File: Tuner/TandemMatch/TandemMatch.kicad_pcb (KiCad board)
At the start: 2 copper layers, 100 x 100 mm, 69 parts, among them J1 Conn_01x02, J10 Conn_01x01, J11 Conn_01x01, J12 Conn_01x01, J13 Conn_01x01, J14 Conn_01x01, J15 Conn_01x01, J16 Conn_01x01, J17 Barrel_Jack, J18 Conn_Coaxial, J19 Conn_01x02, J2 Conn_01x02, J20 Conn_Coaxial, J21 Conn_01x01, J22 Conn_01x01, J23 Conn_01x01, J24 Conn_01x01, J25 Conn_01x01, J26 Conn_01x01, J27 Conn_01x01, J28 Conn_01x01, J29 Conn_01x01, J3 Conn_Coaxial, J30 Conn_01x01, J31 Conn_01x01, J32 Conn_01x01, J33 Conn_01x03, J4 Conn_Coaxial, J5 Conn_01x01, J6 Conn_01x01, J7 Conn_01x01, J8 Conn_01x01, J9 Conn_01x01

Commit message: A few tweaks
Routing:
- net Net-(J11-Pad1): track 60.3 -> 59.1 mm
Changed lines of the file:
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@@
   )
   (setup
-    (last_trace_width 2)
+    (last_trace_width 0.25)
     (user_trace_width 0.35)
     (user_trace_width 0.5)
@@
   (segment (start 129.733 59.182) (end 127.447 56.896) (width 2) (layer B.Cu) (net 2))
   (segment (start 127.447 56.896) (end 127.447 56.957) (width 2) (layer B.Cu) (net 2))
-  (segment (start 127.447 56.957) (end 121.904 62.5) (width 2) (layer B.Cu) (net 2))
-  (segment (start 121.904 62.5) (end 110.50524 62.5) (width 2) (layer B.Cu) (net 2))
+  (segment (start 127.447 56.957) (end 113.4745 62.5475) (width 2) (layer B.Cu) (net 2))
+  (segment (start 113.4745 62.5475) (end 110.50524 62.5) (width 2) (layer B.Cu) (net 2))
   (segment (start 123.19 54.102) (end 124.907 54.356) (width 0.5) (layer B.Cu) (net 2) (status 10))
   (segment (start 124.907 54.356) (end 127.447 56.896) (width 0.5) (layer B.Cu) (net 2))
@@
   (segment (start 111.0234 54.1147) (end 111.0234 51.5747) (width 1) (layer F.Cu) (net 17) (status 30))
   (segment (start 50.038 54.483) (end 50.8 54.483) (width 2) (layer B.Cu) (net 18))
-  (segment (start 50.8 54.483) (end 53.086 56.769) (width 2) (layer B.Cu) (net 18))
-  (segment (start 53.086 56.769) (end 52.766 56.769) (width 2) (layer B.Cu) (net 18))
-  (segment (start 52.766 56.769) (end 53.086 56.769) (width 0.5) (layer B.Cu) (net 18) (status 30))
-  (segment (start 53.086 56.769) (end 56.007 54.356) (width 0.5) (layer B.Cu) (net 18) (status 10))
-  (segment (start 52.766 56.769) (end 53.848 57.404) (width 2) (layer B.Cu) (net 18) (status 10))
-  (segment (start 58.944 62.5) (end 59.293 62.5) (width 2) (layer B.Cu) (net 18))
-  (segment (start 53.848 57.404) (end 58.944 62.5) (width 2) (layer B.Cu) (net 18))
+  (segment (start 50.8 54.483) (end 53.5305 56.7055) (width 2) (layer B.Cu) (net 18))
+  (segment (start 53.5305 56.7055) (end 52.766 56.769) (width 2) (layer B.Cu) (net 18))
+  (segment (start 52.766 56.769) (end 53.5305 56.7055) (width 0.5) (layer B.Cu) (net 18) (status 30))
+  (segment (start 53.5305 56.7055) (end 56.007 54.356) (width 0.5) (layer B.Cu) (net 18) (status 10))
+  (segment (start 52.766 56.769) (end 54.2925 57.3405) (width 2) (layer B.Cu) (net 18) (status 10))
+  (segment (start 65.421 62.4365) (end 65.77 62.4365) (width 2) (layer B.Cu) (net 18))
+  (segment (start 54.2925 57.3405) (end 65.421 62.4365) (width 2) (layer B.Cu) (net 18))
   (segment (start 68.01104 60.03544) (end 68.01104 61.341) (width 0.5) (layer B.Cu) (net 18) (status 10))
   (segment (start 68.01104 61.341) (end 69.17004 62.5) (width 0.5) (layer B.Cu) (net 18))
   (segment (start 75 62.5) (end 69.17004 62.5) (width 2) (layer B.Cu) (net 18) (status 10))
-  (segment (start 69.17004 62.5) (end 59.293 62.5) (width 2) (layer B.Cu) (net 18))
+  (segment (start 69.17004 62.5) (end 65.77 62.4365) (width 2) (layer B.Cu) (net 18))
   (segment (start 52.862 56.865) (end 52.766 56.769) (width 2) (layer B.Cu) (net 18) (status 30))
   (segment (start 49.911 71.12) (end 50.353 71.12) (width 2) (layer B.Cu) (net 19))

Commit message: Actually tuning code now!
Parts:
- added JP7: Jumper_NC_Small, Pin_Headers:Pin_Header_Straight_1x02_Pitch2.54mm, F.Cu at (59.0, 60.1)
- added JP8: Jumper_NC_Small, Pin_Headers:Pin_Header_Straight_1x02_Pitch2.54mm, F.Cu at (123.3, 58.9)
- moved JP6 2.76 mm to (118.9, 51.9), turned to 0 degrees
- moved JP5 1.52 mm to (58.5, 52.8), turned to 0 degrees
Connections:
- J18 pad 1: Net-(J11-Pad1) -> Net-(J18-Pad1)
- J7 pad 1: Net-(J3-Pad1) -> Net-(J7-Pad1)
- JP5 pad 2: Net-(J3-Pad1) -> Net-(J7-Pad1)
- JP9 pad 2: Net-(J3-Pad1) -> Net-(J7-Pad1)
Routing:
- net Net-(J3-Pad1): track 35.8 -> 9.51 mm
- net Net-(J7-Pad1): track 0.00 -> 24.5 mm
- net Net-(J11-Pad1): track 59.1 -> 49.1 mm
- net Net-(J18-Pad1): track 0.00 -> 8.71 mm
- net Net-(JP5-Pad1): track 17.2 -> 18.1 mm
- net Net-(JP6-Pad1): track 23.0 -> 22.3 mm
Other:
- board text added: "ANTENNA"
- board text added: "TRANSMITTER"

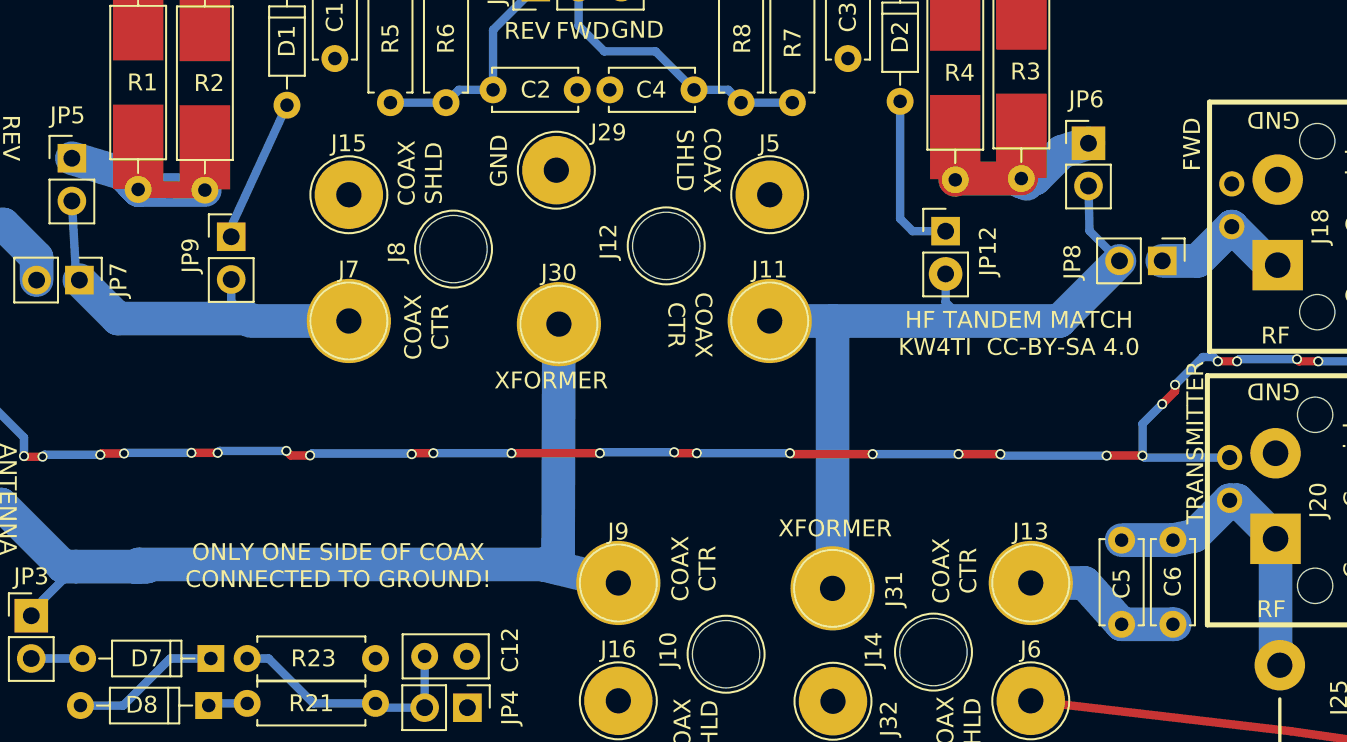
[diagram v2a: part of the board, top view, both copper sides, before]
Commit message: Put level shifters into controller
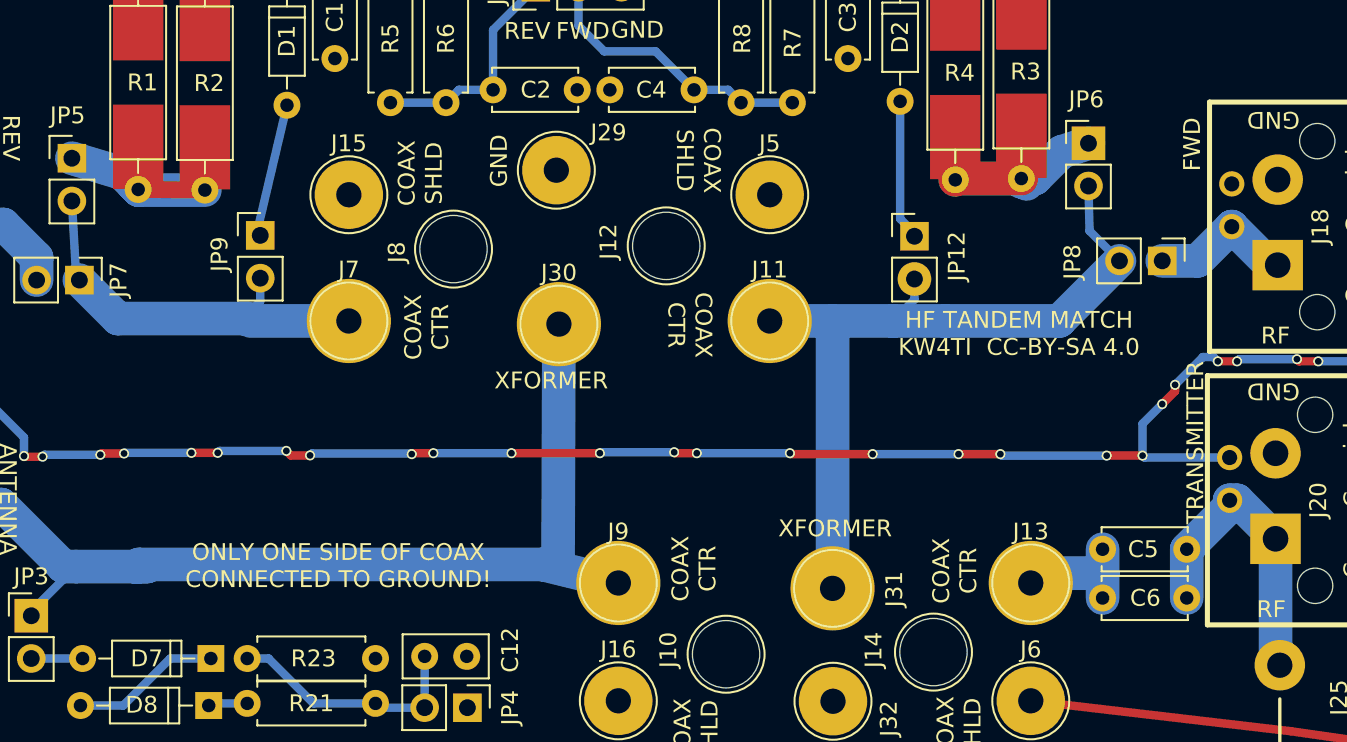
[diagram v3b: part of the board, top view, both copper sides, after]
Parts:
- moved C5 4.60 mm to (119.8, 76.1), turned to 0 degrees
- moved C6 4.46 mm to (119.8, 79.0), turned to 0 degrees
- moved JP12 1.88 mm to (108.6, 57.5)
- moved JP9 1.73 mm to (69.7, 57.4)
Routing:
- net Net-(J11-Pad1): track 49.1 -> 46.7 mm
- net Net-(C5-Pad1): track 9.65 -> 7.40 mm
- net Net-(D2-Pad2): track 10.3 -> 8.64 mm
- net Net-(D1-Pad2): track 8.66 -> 8.02 mm

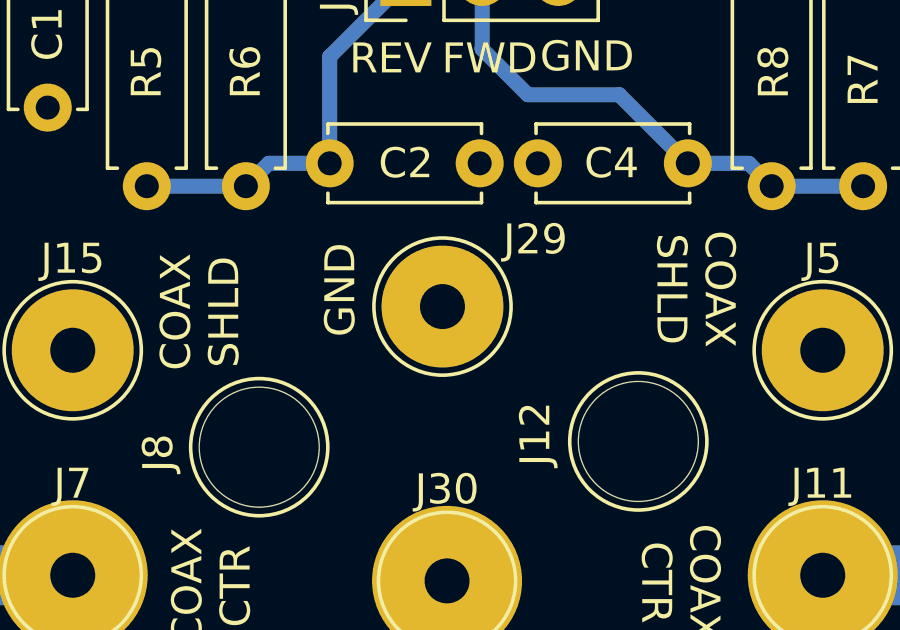
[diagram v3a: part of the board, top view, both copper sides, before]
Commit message: Changed I2C cable pinoutgit add Tunergit add Tuner Also added ICOM rig support
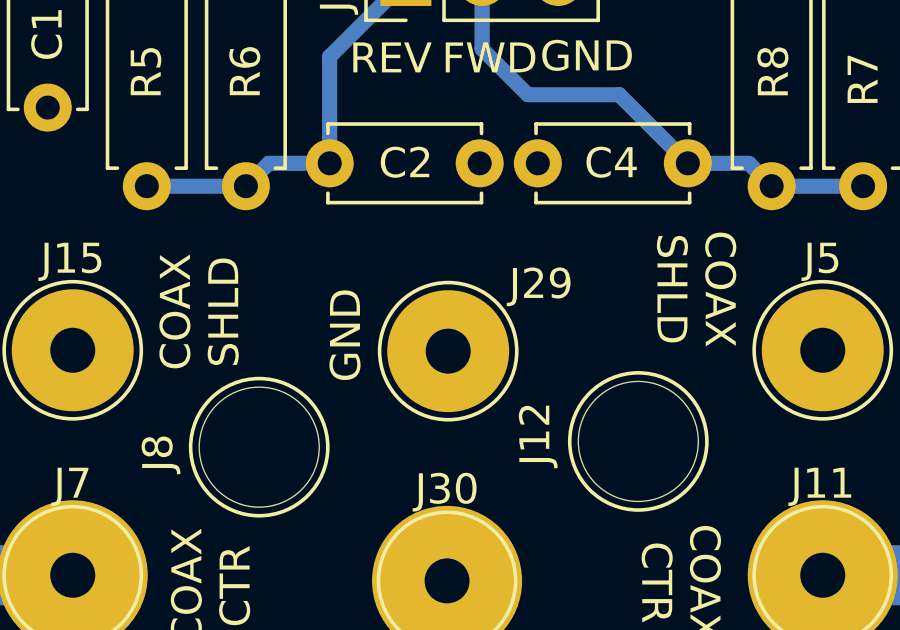
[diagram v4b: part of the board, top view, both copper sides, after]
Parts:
- moved J29 1.50 mm to (87.5, 55.0)
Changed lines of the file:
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@@
   )
   (setup
-    (last_trace_width 0.5)
+    (last_trace_width 0.25)
     (user_trace_width 0.35)
     (user_trace_width 0.5)
@@
   )
   (module Connectors:1pin (layer F.Cu)
-    (at 87.3252 53.5432)
+    (at 87.5157 55.0291)
     (descr "module 1 pin (ou trou mecanique de percage)")
     (tags DEV)
@@
     (effects (font (size 1 1) (thickness 0.15)))
   )
-  (gr_text GND (at 83.9216 52.9844 90) (layer F.SilkS)
+  (gr_text GND (at 84.1121 54.4957 90) (layer F.SilkS)
     (effects (font (size 1 1) (thickness 0.15)))
   )
@@
   (segment (start 122.1486 70.4977) (end 122.2629 70.612) (width 0.5) (layer B.Cu) (net 1))
   (segment (start 90.7415 133.5405) (end 90.7415 132.461) (width 2) (layer B.Cu) (net 1))
-  (segment (start 108.5977 60.0075) (end 108.5977 61.2267) (width 0.5) (layer B.Cu) (net 2) (status 400000))
+  (segment (start 108.5977 60.0075) (end 108.5977 61.2267) (width 0.5) (layer B.Cu) (net 2))
   (segment (start 108.5977 61.2267) (end 107.3244 62.5) (width 0.5) (layer B.Cu) (net 2))
   (segment (start 118.9355 54.483) (end 118.999 57.15) (width 0.5) (layer B.Cu) (net 2) (status 10))
